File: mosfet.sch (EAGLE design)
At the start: 14 parts, among them Q1 BC847CSMD, Q2 BC847CSMD, Q3 BC857CSMD, Q4 IRF530, T1 AO3406, T2 AO3407

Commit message: Update mosfet driver to v3
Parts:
- removed R3: 100k, rcl:R-EU_R0805
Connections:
- net N$3: no longer R3.1
- net N$5: no longer R3.2
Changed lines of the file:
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@@
 <part name="R1" library="rcl" deviceset="R-EU_" device="R0805" value="1k"/>
 <part name="R2" library="rcl" deviceset="R-EU_" device="R0805" value="1k"/>
-<part name="R3" library="rcl" deviceset="R-EU_" device="R0805" value="100k"/>
 <part name="R4" library="rcl" deviceset="R-EU_" device="R0805" value="100k"/>
 <part name="R5" library="rcl" deviceset="R-EU_" device="R0805" value="10"/>
@@
 <instance part="R1" gate="G$1" x="50.8" y="53.34" rot="R90"/>
 <instance part="R2" gate="G$1" x="40.64" y="38.1"/>
-<instance part="R3" gate="G$1" x="35.56" y="30.48" rot="R90"/>
 <instance part="R4" gate="G$1" x="66.04" y="53.34" rot="R90"/>
 <instance part="R5" gate="G$1" x="78.74" y="43.18" rot="R90"/>
@@
 <net name="N$3" class="0">
 <segment>
-<pinref part="R3" gate="G$1" pin="1"/>
 <pinref part="Q2" gate="G$1" pin="E"/>
-<wire x1="35.56" y1="25.4" x2="50.8" y2="25.4" width="0.1524" layer="91"/>
+<wire x1="30.48" y1="25.4" x2="50.8" y2="25.4" width="0.1524" layer="91"/>
 <pinref part="Q3" gate="G$1" pin="C"/>
 <wire x1="50.8" y1="25.4" x2="60.96" y2="25.4" width="0.1524" layer="91"/>
 <junction x="50.8" y="25.4"/>
 <junction x="60.96" y="25.4"/>
-<junction x="35.56" y="25.4"/>
 <pinref part="T1" gate="A" pin="S"/>
 <wire x1="60.96" y1="25.4" x2="78.74" y2="25.4" width="0.1524" layer="91"/>
@@
 <wire x1="25.4" y1="27.94" x2="30.48" y2="27.94" width="0.1524" layer="91"/>
 <wire x1="30.48" y1="27.94" x2="30.48" y2="25.4" width="0.1524" layer="91"/>
-<wire x1="30.48" y1="25.4" x2="35.56" y2="25.4" width="0.1524" layer="91"/>
 <wire x1="93.98" y1="25.4" x2="99.06" y2="25.4" width="0.1524" layer="91"/>
 <junction x="93.98" y="25.4"/>
@@
 <segment>
 <pinref part="R2" gate="G$1" pin="1"/>
-<pinref part="R3" gate="G$1" pin="2"/>
-<wire x1="35.56" y1="38.1" x2="35.56" y2="35.56" width="0.1524" layer="91"/>
-<junction x="35.56" y="38.1"/>
 <wire x1="25.4" y1="30.48" x2="30.48" y2="30.48" width="0.1524" layer="91"/>
 <wire x1="30.48" y1="30.48" x2="30.48" y2="38.1" width="0.1524" layer="91"/>

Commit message: Update mosfet driver to v4
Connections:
- net N$2: now also T2.D; no longer T2.S
- net N$8: now also T2.S; no longer T2.D
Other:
- moved on the sheet: T2
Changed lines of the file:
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@@
 <instance part="Q4" gate="G$1" x="91.44" y="30.48"/>
 <instance part="T1" gate="A" x="78.74" y="30.48"/>
-<instance part="T2" gate="A" x="78.74" y="53.34"/>
+<instance part="T2" gate="A" x="78.74" y="53.34" rot="MR180"/>
 <instance part="JP1" gate="G$1" x="22.86" y="30.48" rot="R180"/>
 <instance part="JP2" gate="A" x="93.98" y="40.64" rot="R270"/>
@@
 <junction x="66.04" y="45.72"/>
 <pinref part="T2" gate="A" pin="G"/>
-<wire x1="73.66" y1="45.72" x2="73.66" y2="50.8" width="0.1524" layer="91"/>
+<wire x1="73.66" y1="45.72" x2="73.66" y2="55.88" width="0.1524" layer="91"/>
 <pinref part="T1" gate="A" pin="G"/>
 <junction x="73.66" y="45.72"/>
-</segment>
-</net>
-<net name="N$2" class="0">
-<segment>
-<pinref part="R5" gate="G$1" pin="2"/>
-<pinref part="T2" gate="A" pin="S"/>
 </segment>
 </net>
@@
 <net name="N$8" class="0">
 <segment>
-<pinref part="JP2" gate="A" pin="4"/>
-<pinref part="R1" gate="G$1" pin="2"/>
+<pinref part="R4" gate="G$1" pin="2"/>
 <pinref part="Q1" gate="G$1" pin="C"/>
-<wire x1="50.8" y1="58.42" x2="60.96" y2="58.42" width="0.1524" layer="91"/>
-<pinref part="R4" gate="G$1" pin="2"/>
 <wire x1="60.96" y1="58.42" x2="66.04" y2="58.42" width="0.1524" layer="91"/>
 <junction x="60.96" y="58.42"/>
-<junction x="66.04" y="58.42"/>
-<pinref part="T2" gate="A" pin="D"/>
+<pinref part="R1" gate="G$1" pin="2"/>
+<wire x1="50.8" y1="58.42" x2="60.96" y2="58.42" width="0.1524" layer="91"/>
+<pinref part="T2" gate="A" pin="S"/>
 <wire x1="66.04" y1="58.42" x2="78.74" y2="58.42" width="0.1524" layer="91"/>
-<wire x1="78.74" y1="58.42" x2="91.44" y2="58.42" width="0.1524" layer="91"/>
-<junction x="78.74" y="58.42"/>
+<pinref part="JP2" gate="A" pin="4"/>
 <pinref part="C2" gate="G$1" pin="1"/>
 <wire x1="91.44" y1="58.42" x2="99.06" y2="58.42" width="0.1524" layer="91"/>
 <wire x1="91.44" y1="43.18" x2="91.44" y2="48.26" width="0.1524" layer="91"/>
-<junction x="91.44" y="58.42"/>
 <pinref part="JP2" gate="A" pin="3"/>
 <wire x1="91.44" y1="48.26" x2="91.44" y2="58.42" width="0.1524" layer="91"/>
@@
 <wire x1="93.98" y1="48.26" x2="91.44" y2="48.26" width="0.1524" layer="91"/>
 <junction x="91.44" y="48.26"/>
+<wire x1="78.74" y1="58.42" x2="91.44" y2="58.42" width="0.1524" layer="91"/>
+<junction x="66.04" y="58.42"/>
+<junction x="78.74" y="58.42"/>
+<junction x="91.44" y="58.42"/>
 </segment>
 </net>
+<net name="N$2" class="0">
+<segment>
+<pinref part="T2" gate="A" pin="D"/>
+<pinref part="R5" gate="G$1" pin="2"/>
+</segment>
+</net>

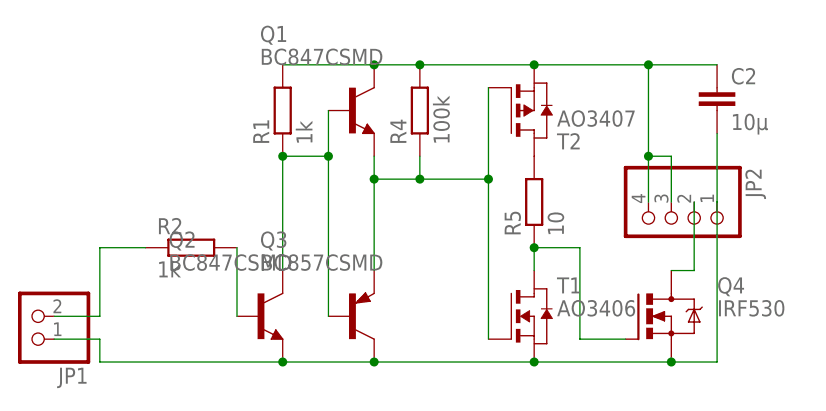
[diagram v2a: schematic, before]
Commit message: Update mosfet driver to v5
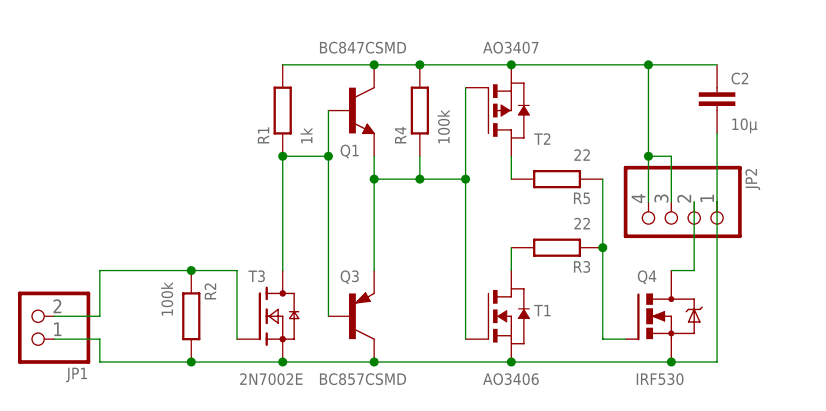
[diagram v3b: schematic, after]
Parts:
- removed Q2: BC847CSMD, transistor-npn:BC847CSMD
- added R3: 22, rcl:R-EU_R0805
- added T3: 2N7002E, nxp_60:2N7002E
- R2: value 1k -> 100k
- R5: value 10 -> 22
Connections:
- removed net N$4: Q2.B, R2.2
- new net N$9: R3.2, T1.D
- net N$1: now also R3.1; no longer T1.D
- net N$3: now also R2.2, T3.S; no longer Q2.E
- net N$5: now also T3.G
- net N$6: now also T3.D; no longer Q2.C
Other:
- moved on the sheet: R2, R5, T1, T2
